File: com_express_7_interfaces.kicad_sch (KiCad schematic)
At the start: 1 part, among them J1 Plug_Bus_CE7_EPT_401-51501-51

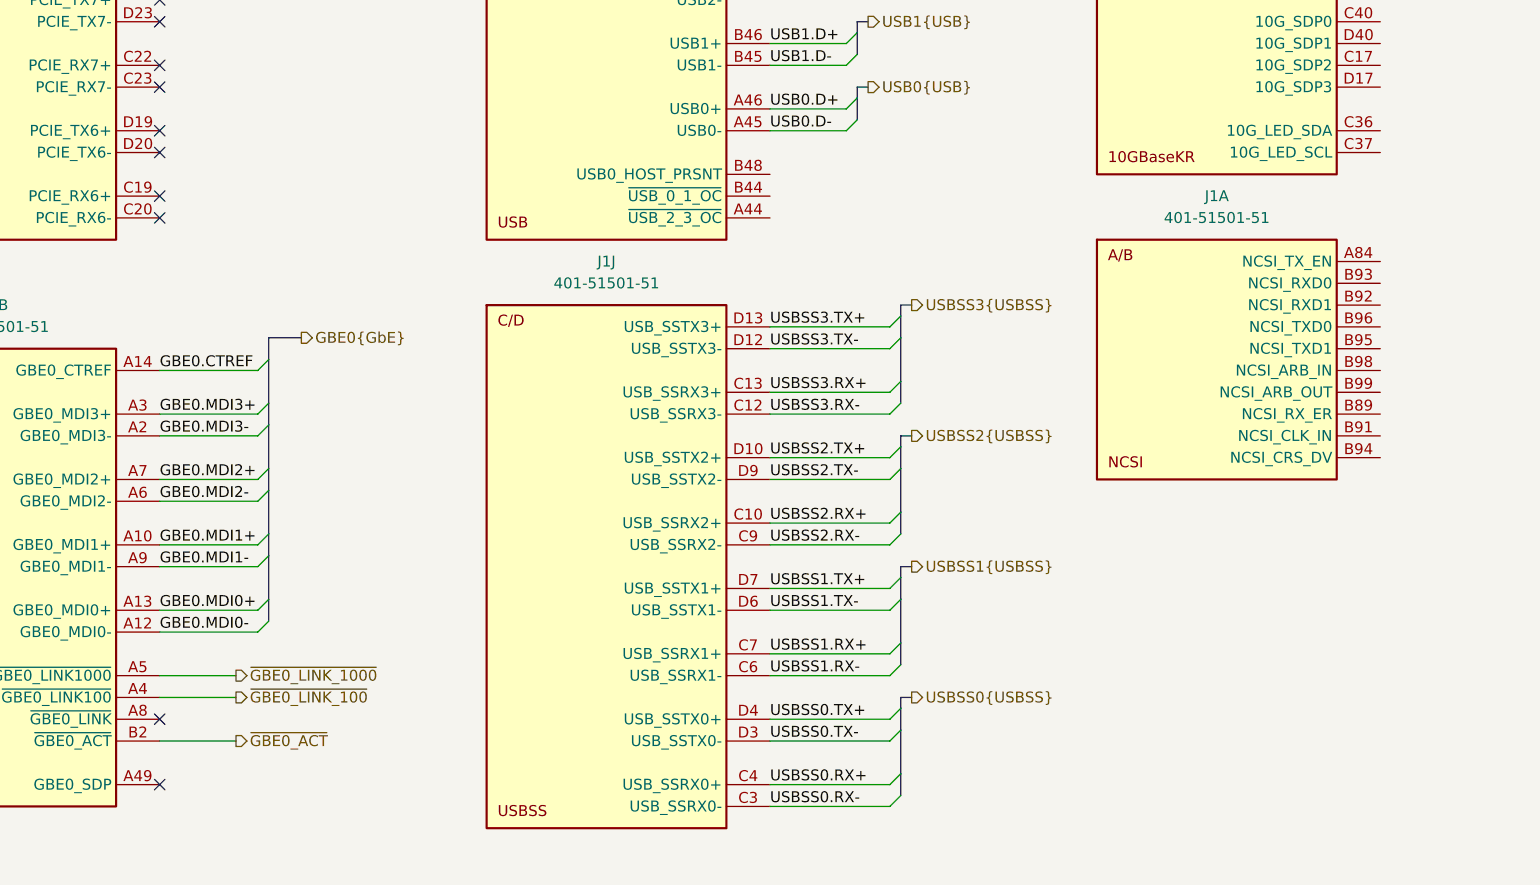
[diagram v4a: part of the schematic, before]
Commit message: [#57056] Update GPIO assignment
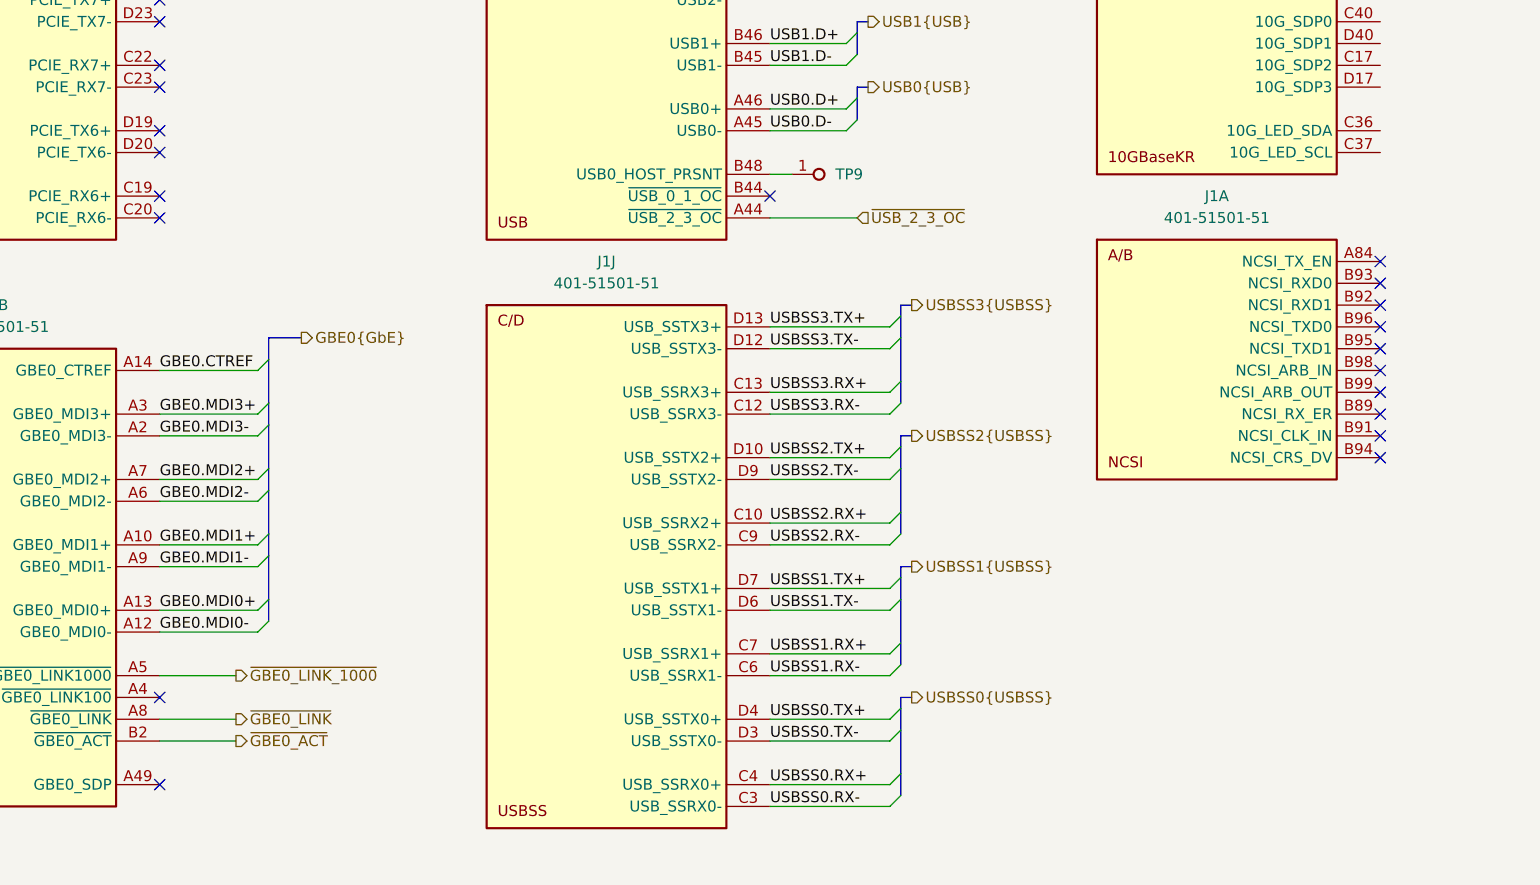
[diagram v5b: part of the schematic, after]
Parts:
- added TP9: TP_0.75mm_SMD, antmicro-footprints:TP_SMD_0.75mm, symbol antmicroTestPoints:TP_0.75mm_SMD
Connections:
- net ~{GBE0_LINK}: now reaches J1.A8 (~{GBE0_LINK})
- net ~{USB_2_3_OC}: now reaches J1.A44 (~{USB_2_3_OC})
- net at J1.B48 (USB0_HOST_PRSNT): now also TP9.1
- net ~{GBE0_LINK_100}: no longer names the net of J1.A4 (~{GBE0_LINK100})
- no-connect marks 58 -> 69
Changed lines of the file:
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@@
   (no_connect (at 68.58 93.98))
   (no_connect (at 68.58 157.48))
+  (no_connect (at 281.94 220.98))
   (no_connect (at 139.7 193.04))
   (no_connect (at 139.7 190.5))
@@
   (no_connect (at 139.7 259.08))
   (no_connect (at 68.58 200.66))
-  (no_connect (at 139.7 251.46))
   (no_connect (at 68.58 81.28))
+  (no_connect (at 281.94 200.66))
   (no_connect (at 68.58 43.18))
   (no_connect (at 68.58 162.56))
+  (no_connect (at 281.94 215.9))
   (no_connect (at 68.58 177.8))
   (no_connect (at 68.58 139.7))
   (no_connect (at 68.58 210.82))
   (no_connect (at 68.58 55.88))
+  (no_connect (at 281.94 218.44))
   (no_connect (at 68.58 149.86))
+  (no_connect (at 139.7 248.92))
   (no_connect (at 68.58 172.72))
   (no_connect (at 68.58 86.36))
@@
   (no_connect (at 139.7 167.64))
   (no_connect (at 68.58 203.2))
+  (no_connect (at 281.94 208.28))
   (no_connect (at 139.7 175.26))
   (no_connect (at 68.58 63.5))
@@
   (no_connect (at 68.58 195.58))
   (no_connect (at 68.58 109.22))
+  (no_connect (at 281.94 203.2))
+  (no_connect (at 281.94 198.12))
   (no_connect (at 68.58 142.24))
+  (no_connect (at 281.94 213.36))
   (no_connect (at 68.58 116.84))
   (no_connect (at 139.7 170.18))
   (no_connect (at 68.58 58.42))
   (no_connect (at 68.58 101.6))
+  (no_connect (at 281.94 210.82))
+  (no_connect (at 281.94 205.74))
   (no_connect (at 68.58 88.9))
   (no_connect (at 68.58 147.32))
@@
   (no_connect (at 68.58 124.46))
   (no_connect (at 68.58 40.64))
+  (no_connect (at 210.82 190.5))
   (no_connect (at 68.58 187.96))
   (bus_entry (at 219.71 180.34) (size 1.27 -1.27)
@@
     (stroke (width 0) (type default))
   )
+  (wire (pts (xy 210.82 193.04) (xy 220.98 193.04))
+    (stroke (width 0) (type default))
+  )
   (bus (pts (xy 156.21 140.97) (xy 156.21 146.05))
     (stroke (width 0) (type default))
@@
     (stroke (width 0) (type default))
   )
+  (wire (pts (xy 213.36 187.96) (xy 210.82 187.96))
+    (stroke (width 0) (type default))
+  )
   (bus (pts (xy 229.87 123.19) (xy 229.87 120.65))
     (stroke (width 0) (type default))
@@
     (stroke (width 0) (type default))
   )
-  (wire (pts (xy 148.59 248.92) (xy 139.7 248.92))
+  (wire (pts (xy 148.59 251.46) (xy 139.7 251.46))
     (stroke (width 0) (type default))
   )
@@
     (effects (font (size 1.27 1.27)) (justify left))
   )
+  (hierarchical_label "~{USB_2_3_OC}" (shape input) (at 220.98 193.04 0) (fields_autoplaced)
+    (effects (font (size 1.27 1.27)) (justify left))
+  )
   (hierarchical_label "KR3{10GBaseKR}" (shape output) (at 297.18 30.48 0) (fields_autoplaced)
     (effects (font (size 1.27 1.27)) (justify left))
@@
     (effects (font (size 1.27 1.27)) (justify left))
   )
-  (hierarchical_label "~{GBE0_LINK_100}" (shape output) (at 148.59 248.92 0) (fields_autoplaced)
+  (hierarchical_label "~{GBE0_LINK}" (shape output) (at 148.59 251.46 0) (fields_autoplaced)
     (effects (font (size 1.27 1.27)) (justify left))
   )
@@
         )
       )
+    )
+  )
+  (symbol (lib_id "antmicroTestPoints:TP_0.75mm_SMD") (at 213.36 187.96 0) (unit 1)
+    (in_bom no) (on_board yes) (dnp no) (fields_autoplaced)
+    (property "Reference" "TP9" (at 218.44 187.96 0)
+      (effects (font (size 1.27 1.27) (thickness 0.15)) (justify left))
+    )
+    (property "Value" "TP_0.75mm_SMD" (at 224.155 191.77 0)
+      (effects (font (size 1.27 1.27) (thickness 0.15)) (justify left bottom) hide)
+    )
+    (property "Footprint" "antmicro-footprints:TP_SMD_0.75mm" (at 224.155 194.31 0)
+      (effects (font (size 1.27 1.27) (thickness 0.15)) (justify left bottom) hide)
+    )
+    (property "Datasheet" "" (at 231.14 200.66 0)
+      (effects (font (size 1.27 1.27) (thickness 0.15)) (justify left bottom) hide)
+    )
+    (property "MPN" "" (at 224.155 199.39 0)
+      (effects (font (size 1.27 1.27) (thickness 0.15)) (justify left bottom) hide)
+    )
+    (property "Manufacturer" "" (at 224.155 194.31 0)
+      (effects (font (size 1.27 1.27) (thickness 0.15)) (justify left bottom) hide)
+    )
+    (property "Author" "Antmicro" (at 224.155 196.85 0)
+      (effects (font (size 1.27 1.27) (thickness 0.15)) (justify left bottom) hide)
+    )
+    (property "License" "Apache-2.0" (at 224.155 199.39 0)
+      (effects (font (size 1.27 1.27) (thickness 0.15)) (justify left bottom) hide)
+    )
+    (pin "1")
+    (instances
+      (project "com-express-7-baseboard"
+        (path "/1b8c34da-dad5-4b0b-8c4b-45db766c4dfa/d0206463-9f0a-4ce9-a6c7-202004597ed5"
+          (reference "TP9") (unit 1)
+        )
+      )

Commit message: [#57498] Add KR/SFP+
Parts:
- added TP37, TP40, TP41, TP42, TP44: TP_0.75mm_SMD, antmicro-footprints:TP_SMD_0.75mm, symbol antmicroTestPoints:TP_0.75mm_SMD
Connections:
- net at J1.C17 (10G_SDP2): now also TP41.1
- net 10G_PHY_RST01: now reaches J1.C35 (10G_PHY_RST_01)
- net I2C_{10GLED}.SDA: now reaches J1.C36 (10G_LED_SDA)
- net I2C_{10GLED}.SCL: now reaches J1.C37 (10G_LED_SCL)
- net I2C_{SFP1}.SDA: now reaches J1.C38 (10G_SFP_SDA1)
- net I2C_{SFP0}.SDA: now reaches J1.C39 (10G_SFP_SDA0)
- net at J1.C40 (10G_SDP0): now also TP37.1
- net MDIO1.MDC: now reaches J1.C45 (10G_PHY_MDC_SCL1)
- net MDIO0.MDC: now reaches J1.C46 (10G_PHY_MDC_SCL0)
- net 10G_INT0: now reaches J1.C47 (10G_INT0)
- net at J1.D17 (10G_SDP3): now also TP42.1
- net at J1.D35 (10G_PHY_CAP_01): now also TP44.1
- net I2C_{SFP1}.SCL: now reaches J1.D38 (10G_SFP_SCL1)
- net I2C_{SFP0}.SCL: now reaches J1.D39 (10G_SFP_SCL0)
- net at J1.D40 (10G_SDP1): now also TP40.1
- net MDIO1.MDIO: now reaches J1.D45 (10G_PHY_MDIO_SDA1)
- net MDIO0.MDIO: now reaches J1.D46 (10G_PHY_MDIO_SDA0)
- net 10G_INT1: now reaches J1.D47 (10G_INT1)
- no-connect marks 69 -> 81
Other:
- note added: "LX2160 SERDES CONFIGURATION: SD1 = 3 SD2 = 3 SD3 = 3"
- note removed: "LX2160 SERDES CONFIGURATION: SD1 = 3 SD2 = 3 SD3 = 2"

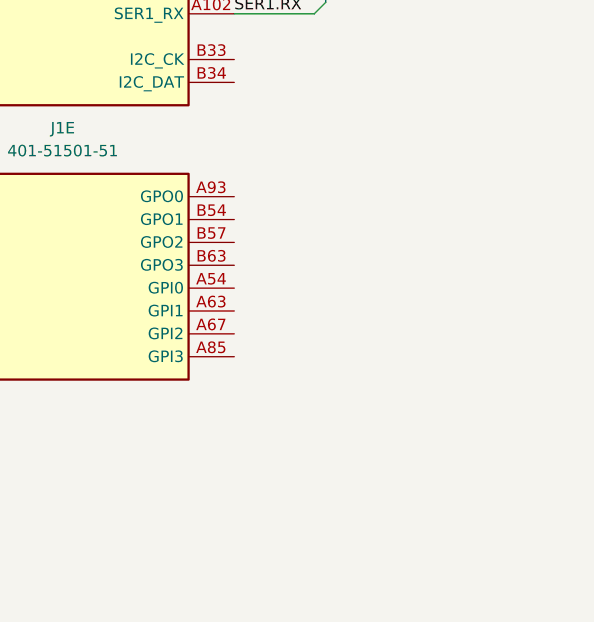
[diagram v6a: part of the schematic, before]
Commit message: [#57498] Add SD card
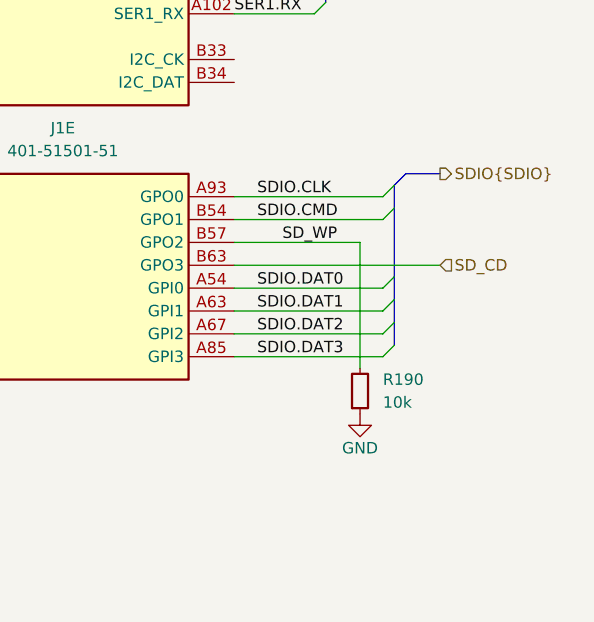
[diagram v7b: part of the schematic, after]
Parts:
- added R190: R_10k_0402, antmicro-footprints:R_0402_1005Metric, symbol antmicroResistors0402:R_10k_0402
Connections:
- net SDIO.DAT0: now reaches J1.A54 (GPI0)
- net SDIO.DAT1: now reaches J1.A63 (GPI1)
- net SDIO.DAT2: now reaches J1.A67 (GPI2)
- net SDIO.DAT3: now reaches J1.A85 (GPI3)
- net SDIO.CLK: now reaches J1.A93 (GPO0)
- net SDIO.CMD: now reaches J1.B54 (GPO1)
- net SD_WP: now reaches J1.B57 (GPO2)
- net SD_WP: now also R190.2
- net SD_CD: now reaches J1.B63 (GPO3)
- new net GND: R190.1

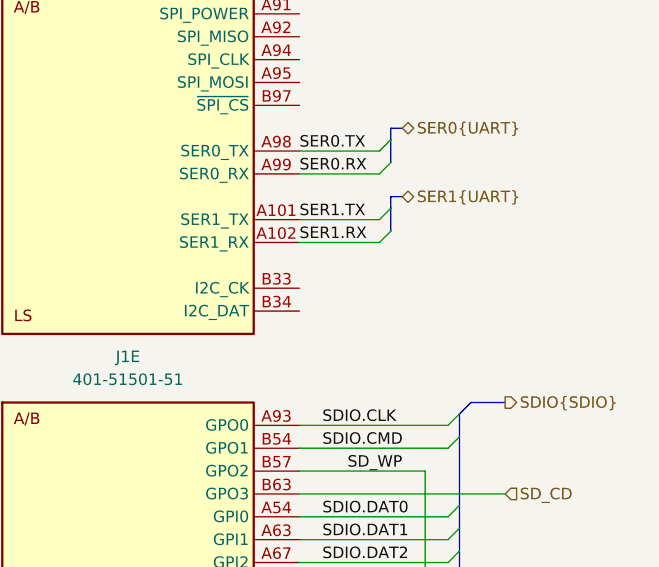
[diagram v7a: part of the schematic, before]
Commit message: [#57056] Add backplane connector
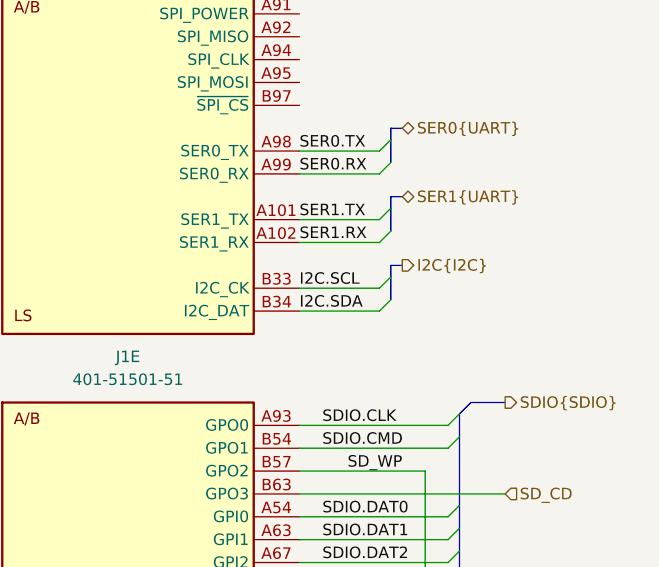
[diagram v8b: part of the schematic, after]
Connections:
- net I2C.SCL: now reaches J1.B33 (I2C_CK)
- net I2C.SDA: now reaches J1.B34 (I2C_DAT)
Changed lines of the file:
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@@
+    (stroke (width 0) (type default))
+  )
+  (bus_entry (at 363.22 107.95) (size -1.27 1.27)
     (stroke (width 0) (type default))
   )
@@
     (stroke (width 0) (type default))
   )
+  (bus_entry (at 363.22 105.41) (size -1.27 1.27)
+    (stroke (width 0) (type default))
+  )
   (bus_entry (at 299.72 118.11) (size -1.27 1.27)
     (stroke (width 0) (type default))
@@
     (stroke (width 0) (type default))
   )
+  (wire (pts (xy 361.95 106.68) (xy 353.06 106.68))
+    (stroke (width 0) (type default))
+  )
   (bus (pts (xy 156.21 31.75) (xy 156.21 34.29))
     (stroke (width 0) (type default))
@@
     (stroke (width 0) (type default))
   )
+  (wire (pts (xy 361.95 109.22) (xy 353.06 109.22))
+    (stroke (width 0) (type default))
+  )
   (bus (pts (xy 370.84 123.19) (xy 370.84 130.81))
     (stroke (width 0) (type default))
@@
     (stroke (width 0) (type default))
   )
+  (bus (pts (xy 363.22 104.14) (xy 364.49 104.14))
+    (stroke (width 0) (type default))
+  )
   (wire (pts (xy 210.82 254) (xy 224.79 254))
     (stroke (width 0) (type default))
@@
     (stroke (width 0) (type default))
   )
+  (bus (pts (xy 363.22 105.41) (xy 363.22 107.95))
+    (stroke (width 0) (type default))
+  )
   (bus (pts (xy 299.72 120.65) (xy 299.72 123.19))
     (stroke (width 0) (type default))
@@
   )
   (wire (pts (xy 210.82 55.88) (xy 228.6 55.88))
+    (stroke (width 0) (type default))
+  )
+  (bus (pts (xy 363.22 105.41) (xy 363.22 104.14))
     (stroke (width 0) (type default))
   )
@@
     (effects (font (size 1.27 1.27)) (justify left bottom))
   )
+  (label "I2C.SCL" (at 353.06 106.68 0) (fields_autoplaced)
+    (effects (font (size 1.27 1.27)) (justify left bottom))
+  )
   (label "PCIe_{B2Bx4}.RX3+" (at 139.7 40.64 0) (fields_autoplaced)
     (effects (font (size 1.27 1.27)) (justify left bottom))
@@
     (effects (font (size 1.27 1.27)) (justify left bottom))
   )
+  (label "I2C.SDA" (at 353.06 109.22 0) (fields_autoplaced)
+    (effects (font (size 1.27 1.27)) (justify left bottom))
+  )
   (label "I2C_{SFP0}.SDA" (at 298.45 101.6 180) (fields_autoplaced)
     (effects (font (size 1.27 1.27)) (justify right bottom))
@@
     (effects (font (size 1.27 1.27)) (justify left))
   )
+  (hierarchical_label "I2C{I2C}" (shape output) (at 364.49 104.14 0) (fields_autoplaced)
+    (effects (font (size 1.27 1.27)) (justify left))
+  )
